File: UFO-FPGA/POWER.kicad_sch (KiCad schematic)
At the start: 41 parts, among them J5 USB_B_Micro, Q1 2N7002

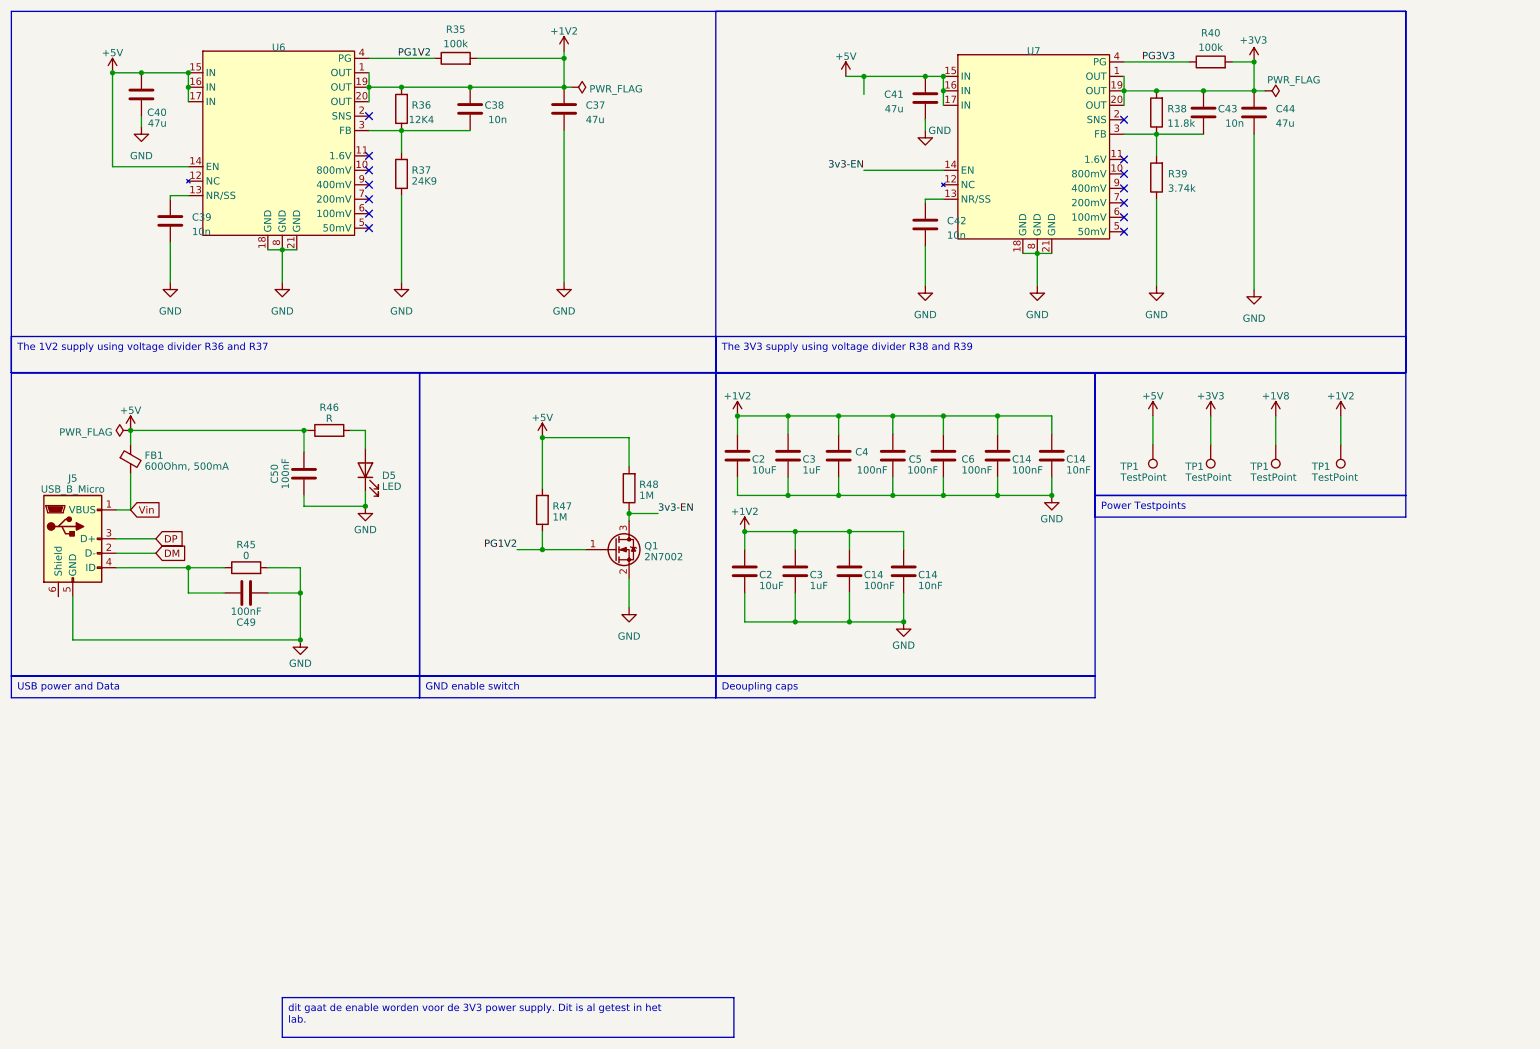
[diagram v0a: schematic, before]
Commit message: Opamp gemaakt van de ADC
Enkel nog begrijpen wat VDC is. Aan docent vragen?
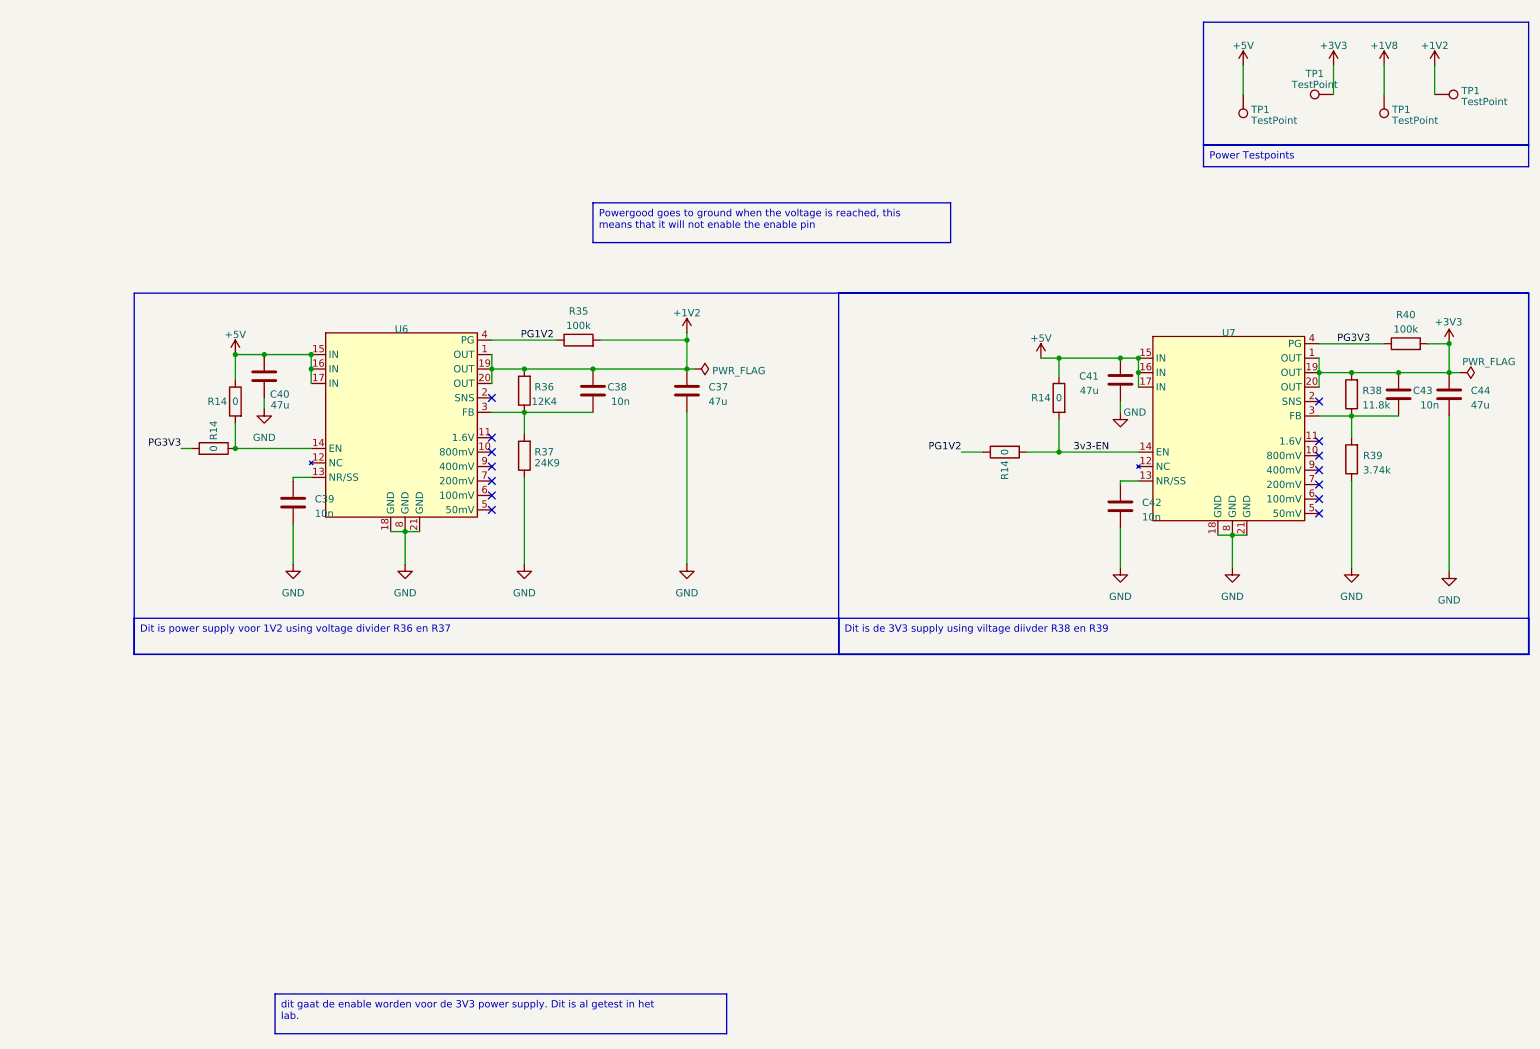
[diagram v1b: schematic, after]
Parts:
- removed C14 (x2), C4, C49, C5, C50, C6: 100nF, symbol Device:C
- removed C14 (x2): 10nF, symbol Device:C
- removed C2 (x2): 10uF, symbol Device:C
- removed C3 (x2): 1uF, symbol Device:C
- removed D5: LED, symbol Device:LED
- removed FB1: 600Ohm, 500mA, symbol Device:FerriteBead_Small
- removed J5: USB_B_Micro, symbol Connector:USB_B_Micro
- removed Q1: 2N7002, Package_TO_SOT_SMD:SOT-23, symbol Transistor_FET:2N7002
- removed R45: 0, symbol Device:R
- removed R46: R, symbol Device:R
- removed R47, R48: 1M, symbol Device:R
- removed TP1 (x4): TestPoint, symbol Connector:TestPoint
- added R14 (x4): 0, symbol Device:R
- added TP1 (x4): TestPoint, symbol Connector:TestPoint
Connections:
- net +1V2: now also TP1.1
- net +1V8: now also TP1.1
- net +3V3: now also TP1.1
- net +5V: now also R14.1, R14.1, TP1.1; no longer U6.14 (EN)
- net 3v3-EN: now also R14.2, R14.2
- net PG1V2: now also R14.1
- net PG3V3: now also R14.2
- new net: R14.1, R14.2, U6.14 (EN)

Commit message: Fixed text and placement
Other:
- moved on the sheet: C37, C38, C39, C40, C41, C42, C43, C44, R14, R35, R36, R37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

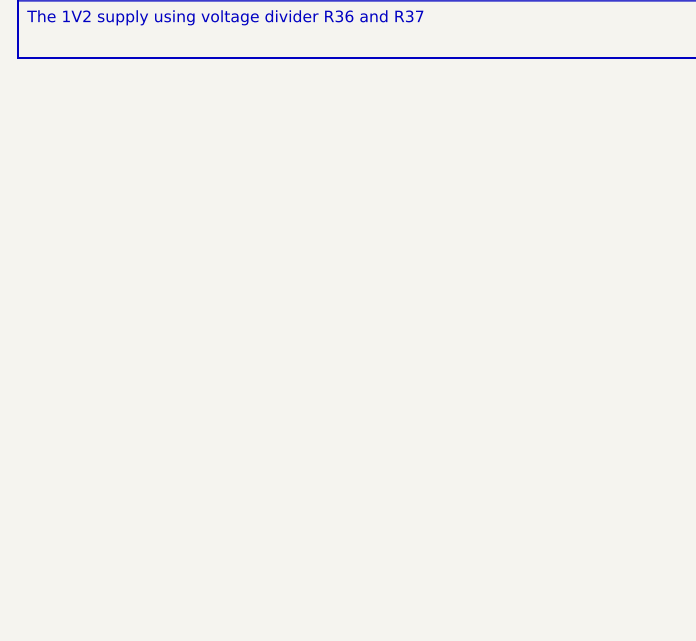
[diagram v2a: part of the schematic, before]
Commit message: pins and USB
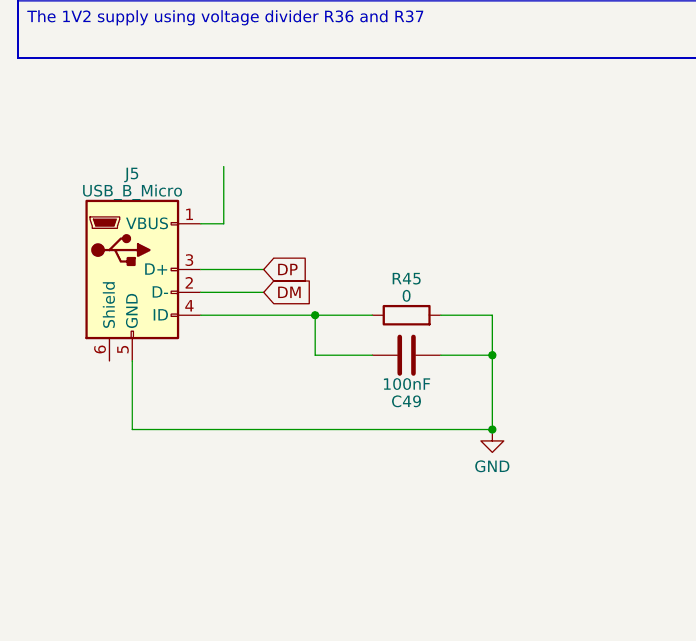
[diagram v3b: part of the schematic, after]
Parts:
- added C49: 100nF, symbol Device:C
- added J5: USB_B_Micro, symbol Connector:USB_B_Micro
- added R45: 0, symbol Device:R
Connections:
- net GND: now also C49.2, J5.5 (GND), R45.2
- new net: C49.1, J5.4 (ID), R45.1
- new net DM: J5.2 (D-)
- new net DP: J5.3 (D+)
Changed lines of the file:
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@@
   (junction (at 107.95 20.955) (diameter 0) (color 0 0 0 0)
   )
+  (junction (at 63.5 117.475) (diameter 0) (color 0 0 0 0)
+  )
   (junction (at 91.44 26.035) (diameter 0) (color 0 0 0 0)
   )
@@
   (junction (at 184.15 24.13) (diameter 0) (color 0 0 0 0)
   )
+  (junction (at 43.815 104.775) (diameter 0) (color 0 0 0 0)
+  )
   (junction (at 107.95 26.035) (diameter 0) (color 0 0 0 0)
   )
@@
   )
   (junction (at 173.355 40.64) (diameter 0) (color 0 0 0 0)
+  )
+  (junction (at 63.5 109.22) (diameter 0) (color 0 0 0 0)
   )
   (junction (at 241.935 21.59) (diameter 0) (color 0 0 0 0)
@@
     (stroke (width 0) (type default))
   )
+  (wire (pts (xy 31.115 102.235) (xy 38.1 102.235))
+    (stroke (width 0) (type default))
+  )
   (wire (pts (xy 241.935 34.29) (xy 241.935 61.595))
     (stroke (width 0) (type default))
@@
     (stroke (width 0) (type default))
   )
+  (wire (pts (xy 43.815 104.775) (xy 50.165 104.775))
+    (stroke (width 0) (type default))
+  )
   (wire (pts (xy 173.355 34.925) (xy 173.355 40.64))
     (stroke (width 0) (type default))
@@
     (stroke (width 0) (type default))
   )
+  (wire (pts (xy 31.115 99.695) (xy 38.1 99.695))
+    (stroke (width 0) (type default))
+  )
   (wire (pts (xy 219.075 26.67) (xy 224.79 26.67))
     (stroke (width 0) (type default))
@@
     (stroke (width 0) (type default))
   )
+  (wire (pts (xy 33.655 88.265) (xy 33.655 94.615))
+    (stroke (width 0) (type default))
+  )
   (wire (pts (xy 92.71 20.955) (xy 107.95 20.955))
     (stroke (width 0) (type default))
@@
     (stroke (width 0) (type default))
   )
+  (wire (pts (xy 63.5 109.22) (xy 63.5 117.475))
+    (stroke (width 0) (type default))
+  )
+  (wire (pts (xy 23.495 117.475) (xy 63.5 117.475))
+    (stroke (width 0) (type default))
+  )
   (wire (pts (xy 79.375 33.655) (xy 79.375 37.465))
     (stroke (width 0) (type default))
@@
     (stroke (width 0) (type default))
   )
+  (wire (pts (xy 63.5 104.775) (xy 63.5 109.22))
+    (stroke (width 0) (type default))
+  )
+  (wire (pts (xy 31.115 104.775) (xy 43.815 104.775))
+    (stroke (width 0) (type default))
+  )
+  (wire (pts (xy 57.785 104.775) (xy 63.5 104.775))
+    (stroke (width 0) (type default))
+  )
   (wire (pts (xy 173.355 40.64) (xy 187.325 40.64))
     (stroke (width 0) (type default))
@@
     (stroke (width 0) (type default))
   )
+  (wire (pts (xy 31.115 94.615) (xy 33.655 94.615))
+    (stroke (width 0) (type default))
+  )
+  (wire (pts (xy 50.165 109.22) (xy 43.815 109.22))
+    (stroke (width 0) (type default))
+  )
   (wire (pts (xy 187.325 24.13) (xy 187.325 26.67))
     (stroke (width 0) (type default))
@@
     (stroke (width 0) (type default))
   )
+  (wire (pts (xy 57.785 109.22) (xy 63.5 109.22))
+    (stroke (width 0) (type default))
+  )
   (wire (pts (xy 166.37 85.09) (xy 166.37 90.17))
     (stroke (width 0) (type default))
@@
     (stroke (width 0) (type default))
   )
+  (wire (pts (xy 43.815 109.22) (xy 43.815 104.775))
+    (stroke (width 0) (type default))
+  )
   (wire (pts (xy 173.355 24.13) (xy 184.15 24.13))
     (stroke (width 0) (type default))
@@
   )
   (wire (pts (xy 107.95 20.955) (xy 107.95 26.035))
+    (stroke (width 0) (type default))
+  )
+  (wire (pts (xy 23.495 109.855) (xy 23.495 117.475))
     (stroke (width 0) (type default))
   )
@@
     (effects (font (size 1.27 1.27)) (justify left bottom))
   )
+  (global_label "DP" (shape input) (at 38.1 99.695 0) (fields_autoplaced)
+    (effects (font (size 1.27 1.27)) (justify left))
+    (property "Intersheetrefs" "${INTERSHEET_REFS}" (at 43.5458 99.695 0)
+      (effects (font (size 1.27 1.27)) (justify left) hide)
+    )
+  )
+  (global_label "DM" (shape input) (at 38.1 102.235 0) (fields_autoplaced)
+    (effects (font (size 1.27 1.27)) (justify left))
+    (property "Intersheetrefs" "${INTERSHEET_REFS}" (at 43.7272 102.235 0)
+      (effects (font (size 1.27 1.27)) (justify left) hide)
+    )
+  )
+  (symbol (lib_id "Device:R") (at 53.975 104.775 90) (unit 1)
+    (in_bom yes) (on_board yes) (dnp no) (fields_autoplaced)
+    (property "Reference" "R45" (at 53.975 100.7491 90)
+      (effects (font (size 1.27 1.27)))
+    )
+    (property "Value" "0" (at 53.975 102.6701 90)
+      (effects (font (size 1.27 1.27)))
+    )
+    (property "Footprint" "" (at 53.975 106.553 90)
+      (effects (font (size 1.27 1.27)) hide)
+    )
+    (property "Datasheet" "~" (at 53.975 104.775 0)
+      (effects (font (size 1.27 1.27)) hide)
+    )
+    (pin "1")
+    (pin "2")
+    (instances
+      (project "UFO-FPGA"
+        (path "/b3168f6a-c732-41d3-aeeb-d97dd2f1bb65/abe08156-b909-4d2d-ad35-f723f4a728d5"
+          (reference "R45") (unit 1)
+        )
+      )
+    )
+  )
   (symbol (lib_id "Device:C") (at 107.95 29.845 0) (unit 1)
     (in_bom yes) (on_board yes) (dnp no) (fields_autoplaced)
@@
     )
   )
+  (symbol (lib_id "Device:C") (at 53.975 109.22 90) (mirror x) (unit 1)
+    (in_bom yes) (on_board yes) (dnp no)
+    (property "Reference" "C49" (at 53.975 114.3889 90)
+      (effects (font (size 1.27 1.27)))
+    )
+    (property "Value" "100nF" (at 53.975 112.4679 90)
+      (effects (font (size 1.27 1.27)))
+    )
+    (property "Footprint" "" (at 57.785 110.1852 0)
+      (effects (font (size 1.27 1.27)) hide)
+    )
+    (property "Datasheet" "~" (at 53.975 109.22 0)
+      (effects (font (size 1.27 1.27)) hide)
+    )
+    (pin "1")
+    (pin "2")
+    (instances
+      (project "UFO-FPGA"
+        (path "/b3168f6a-c732-41d3-aeeb-d97dd2f1bb65/abe08156-b909-4d2d-ad35-f723f4a728d5"
+          (reference "C49") (unit 1)
+        )
+      )
+    )
+  )
   (symbol (lib_id "Device:R") (at 173.355 31.115 0) (mirror y) (unit 1)
     (in_bom yes) (on_board yes) (dnp no)
@@
         (path "/b3168f6a-c732-41d3-aeeb-d97dd2f1bb65/abe08156-b909-4d2d-ad35-f723f4a728d5"
           (reference "C43") (unit 1)
+        )
+      )
+    )
+  )
+  (symbol (lib_id "power:GND") (at 63.5 117.475 0) (unit 1)
+    (in_bom yes) (on_board yes) (dnp no) (fields_autoplaced)
+    (property "Reference" "#PWR063" (at 63.5 123.825 0)
+      (effects (font (size 1.27 1.27)) hide)
+    )
+    (property "Value" "GND" (at 63.5 121.6105 0)
+      (effects (font (size 1.27 1.27)))
+    )
+    (property "Footprint" "" (at 63.5 117.475 0)
+      (effects (font (size 1.27 1.27)) hide)
+    )
+    (property "Datasheet" "" (at 63.5 117.475 0)
+      (effects (font (size 1.27 1.27)) hide)
+    )
+    (pin "1")
+    (instances
+      (project "UFO-FPGA"
+        (path "/b3168f6a-c732-41d3-aeeb-d97dd2f1bb65/abe08156-b909-4d2d-ad35-f723f4a728d5"
+          (reference "#PWR063") (unit 1)
         )
       )
@@
         )
       )
+    )
+  )
+  (symbol (lib_id "Connector:USB_B_Micro") (at 23.495 99.695 0) (unit 1)
+    (in_bom yes) (on_board yes) (dnp no) (fields_autoplaced)
+    (property "Reference" "J5" (at 23.495 89.0651 0)
+      (effects (font (size 1.27 1.27)))
+    )
+    (property "Value" "USB_B_Micro" (at 23.495 90.9861 0)
+      (effects (font (size 1.27 1.27)))
+    )
+    (property "Footprint" "" (at 27.305 100.965 0)
+      (effects (font (size 1.27 1.27)) hide)
+    )
+    (property "Datasheet" "~" (at 27.305 100.965 0)
+      (effects (font (size 1.27 1.27)) hide)
+    )
+    (pin "1")
+    (pin "2")
+    (pin "3")
+    (pin "4")
+    (pin "5")
+    (pin "6")
+    (instances
+      (project "UFO-FPGA"
+        (path "/b3168f6a-c732-41d3-aeeb-d97dd2f1bb65/abe08156-b909-4d2d-ad35-f723f4a728d5"
+          (reference "J5") (unit 1)
+        )
+      )

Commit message: De inverting supply schakeling gemaakt
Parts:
- removed C49: 100nF, symbol Device:C
- removed J5: USB_B_Micro, symbol Connector:USB_B_Micro
- removed R45: 0, symbol Device:R
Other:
- moved on the sheet: C37, C38, C39, C40, C41, C42, C43, C44, R14, R35, R36, R37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

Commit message: IO and power
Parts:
- removed R14 (x4): 0, symbol Device:R
- removed TP1 (x4): TestPoint, symbol Connector:TestPoint
- added C14 (x2): 10nF, symbol Device:C
- added C14 (x2), C4, C49, C5, C50, C6: 100nF, symbol Device:C
- added C2 (x2): 10uF, symbol Device:C
- added C3 (x2): 1uF, symbol Device:C
- added D5: LED, symbol Device:LED
- added FB1: 600Ohm, 500mA, symbol Device:FerriteBead_Small
- added J5: USB_B_Micro, symbol Connector:USB_B_Micro
- added Q1: 2N7002, Package_TO_SOT_SMD:SOT-23, symbol Transistor_FET:2N7002
- added R45: 0, symbol Device:R
- added R46: R, symbol Device:R
- added R47, R48: 1M, symbol Device:R
- added TP1 (x4): TestPoint, symbol Connector:TestPoint
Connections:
- net +1V2: now also C14.1, C14.1, C14.1, C14.1, C2.1, C2.1, C3.1, C3.1, C4.1, C5.1, C6.1, TP1.1
- net +1V8: now also TP1.1
- net +3V3: now also TP1.1
- net +5V: now also U6.14 (EN), C50.1, FB1.1, R46.1, R47.2, R48.2, TP1.1
- net 3v3-EN: now also Q1.3 (D), R48.1
- net GND: now also C14.2, C14.2, C14.2, C14.2, C2.2, C2.2, C3.2, C3.2, C4.2, C49.2, C5.2, C50.2, C6.2, D5.1 (K), J5.5 (GND), Q1.2 (S), R45.2
- net PG1V2: now also Q1.1 (G), R47.1
- new net: C49.1, J5.4 (ID), R45.1
- new net: D5.2 (A), R46.2
- new net DM: J5.2 (D-)
- new net DP: J5.3 (D+)
- new net Vin: FB1.2, J5.1 (VBUS)

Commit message: Revision
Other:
- company: (none) -> Universal-Field-Objects
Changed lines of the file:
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@@
   (title_block
     (title "UFO FPGA")
-    (date "2023-04-22")
-    (rev "V0.1")
+    (date "2023-04-25")
+    (rev "V0.5")
+    (company "Universal-Field-Objects")
   )
   (junction (at 161.925 106.68) (diameter 0) (color 0 0 0 0)
